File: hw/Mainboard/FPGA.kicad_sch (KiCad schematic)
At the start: 60 parts, among them J16 MCU, J19 PROG, J21 FPGA-P4, J23 FPGA_P2, J24 Conn_02x15_Odd_Even, Q4 MMBT3904, SW5 CONFIG, U21 T8Q144C3

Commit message: hw: add more Mouse part numbers
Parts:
- J16: value MCU -> FPGA_MCU; MOUSER (none) -> 649-1012938195002BLF
- J21: value FPGA-P4 -> FPGA_P3; MOUSER (none) -> 649-1012938195002BLF
- J23: MOUSER (none) -> 649-1012938195002BLF
- J24: value Conn_02x15_Odd_Even -> FPGA_P1; MOUSER (none) -> 649-1012938195002BLF
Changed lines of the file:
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@@
       (effects (font (size 1.27 1.27)) (justify right))
     )
-    (property "Value" "FPGA-P4" (id 1) (at 356.87 152.4 90)
+    (property "Value" "FPGA_P3" (id 1) (at 356.87 152.4 90)
       (effects (font (size 1.27 1.27)) (justify right))
     )
@@
       (effects (font (size 1.27 1.27)) hide)
     )
-    (property "MOUSER" "" (id 5) (at 382.27 162.56 0)
+    (property "MOUSER" "649-1012938195002BLF" (id 5) (at 382.27 162.56 0)
       (effects (font (size 1.27 1.27)) hide)
     )
@@
       (effects (font (size 1.27 1.27)) hide)
     )
-    (property "MOUSER" "" (id 5) (at 384.81 57.15 0)
+    (property "MOUSER" "649-1012938195002BLF" (id 5) (at 384.81 57.15 0)
       (effects (font (size 1.27 1.27)) hide)
     )
@@
     (in_bom yes) (on_board yes) (fields_autoplaced)
     (property "Reference" "J24" (id 0) (at 383.54 82.55 0))
-    (property "Value" "Conn_02x15_Odd_Even" (id 1) (at 383.54 85.09 0))
+    (property "Value" "FPGA_P1" (id 1) (at 383.54 85.09 0))
     (property "Footprint" "Connector_PinHeader_2.54mm:PinHeader_2x15_P2.54mm_Vertical" (id 2) (at 382.27 106.68 0)
       (effects (font (size 1.27 1.27)) hide)
     )
     (property "Datasheet" "" (id 3) (at 382.27 106.68 0)
+      (effects (font (size 1.27 1.27)) hide)
+    )
+    (property "MOUSER" "649-1012938195002BLF" (id 4) (at 382.27 106.68 0)
       (effects (font (size 1.27 1.27)) hide)
     )
@@
     (in_bom yes) (on_board yes) (fields_autoplaced)
     (property "Reference" "J16" (id 0) (at 210.82 35.56 0))
-    (property "Value" "MCU" (id 1) (at 210.82 38.1 0))
+    (property "Value" "FPGA_MCU" (id 1) (at 210.82 38.1 0))
     (property "Footprint" "Connector_PinHeader_2.54mm:PinHeader_2x11_P2.54mm_Vertical" (id 2) (at 209.55 53.34 0)
       (effects (font (size 1.27 1.27)) hide)
@@
       (effects (font (size 1.27 1.27)) hide)
     )
+    (property "MOUSER" "649-1012938195002BLF" (id 4) (at 209.55 53.34 0)
+      (effects (font (size 1.27 1.27)) hide)
+    )

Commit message: hw: PN for IC, remove dup PNs, remove redundant headroom text on PWR
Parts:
- J21, J23: DIGI-KEY SAM1204-14-ND -> (none)
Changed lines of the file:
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@@
-      (effects (font (size 1.27 1.27)) hide)
-    )
-    (property "DIGI-KEY" "SAM1204-14-ND" (id 4) (at 382.27 162.56 0)
       (effects (font (size 1.27 1.27)) hide)
     )
@@
       (effects (font (size 1.27 1.27)) hide)
     )
-    (property "DIGI-KEY" "SAM1204-14-ND" (id 4) (at 384.81 57.15 0)
-      (effects (font (size 1.27 1.27)) hide)
-    )

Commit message: hw: 9V DC plug on left edge, change default track size
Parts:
- renumbered C74 to C31, C60 to C32, C83 to C33, C61 to C34, C66 to C35, C68 to C36, C64 to C37, C63 to C38, C65 to C39, C62 to C40, C67 to C41, C53 to C42, C75 to C43, C71 to C44, C72 to C45, C78 to C46, C34 to C47, C76 to C48, C77 to C49, C79 to C50, C80 to C51, C69 to C52, C73 to C53, D8 to D10, D9 to D11, J19 to J5, J16 to J6, J23 to J7, J24 to J8, J21 to J9, PT41 to PT15, PT42 to PT16, PT43 to PT17, PT44 to PT18, PT45 to PT19, PT46 to PT20, PT48 to PT21, PT47 to PT22, PT40 to PT23, PT54 to PT24, PT53 to PT25, PT52 to PT26, PT51 to PT27, PT50 to PT28, PT49 to PT29, PT39 to PT30, Q4 to Q1, R27 to R20, R33 to R21, R70 to R22, R68 to R23, R71 to R24, R34 to R25, R29 to R26, R30 to R27, R31 to R28, RN14 to RN1, RN15 to RN2, SW5 to SW3, U21 to U10
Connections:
- net GND: no longer PT30.2, U10.1 (GND), U10.104 (GND), U10.108 (GND), U10.120 (GND), U10.121 (GND), U10.126 (GND), U10.127 (GND), U10.129 (GND), U10.133 (GND), U10.37 (GND), U10.44 (GND), U10.5 (GND), U10.50 (GND), U10.64 (GND), U10.9 (GND), U10.94 (GND)
- new net VSS: PT30.2, U10.1 (GND), U10.104 (GND), U10.108 (GND), U10.120 (GND), U10.121 (GND), U10.126 (GND), U10.127 (GND), U10.129 (GND), U10.133 (GND), U10.37 (GND), U10.44 (GND), U10.5 (GND), U10.50 (GND), U10.64 (GND), U10.9 (GND), U10.94 (GND)

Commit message: hw: 25x2 header (wip)
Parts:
- removed J7: FPGA_P2, Connector_PinHeader_2.54mm:PinHeader_2x14_P2.54mm_Vertical, symbol Connector_Generic:Conn_02x14_Odd_Even
- removed J8: FPGA_P1, Connector_PinHeader_2.54mm:PinHeader_2x15_P2.54mm_Vertical, symbol Connector_Generic:Conn_02x15_Odd_Even
- removed J9: FPGA_P3, Connector_PinHeader_2.54mm:PinHeader_2x14_P2.54mm_Vertical, symbol Connector_Generic:Conn_02x14_Odd_Even
- added J5: PMOD1, PET:PMOD_Socket_2x06_P2.54mm_Horizontal, symbol Connector_Generic:Conn_02x06_Top_Bottom
- added J6: PMOD2, PET:PMOD_Socket_2x06_P2.54mm_Horizontal, symbol Connector_Generic:Conn_02x06_Top_Bottom
- added J9: BUS_EXPANSION, Connector_PinHeader_2.54mm:PinHeader_2x25_P2.54mm_Vertical, symbol Connector_Generic:Conn_02x25_Odd_Even
- renumbered J5 to J7, J6 to J8
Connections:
- net +3V3: now also J5.12 (Pin_12), J5.6 (Pin_6), J6.12 (Pin_12), J6.6 (Pin_6), J9.2 (Pin_2)
- net A0: now also U10.58 (GPIOB_RXP02), J9.15 (Pin_15); no longer U10.70 (GPIOB_RXP12_EXTFB0)
- net A1: now also U10.60 (GPIOB_RXN03), J9.17 (Pin_17); no longer U10.72 (GPIOB_CLKN0)
- net A10: now also U10.92 (GPIOR_125_CLK10), J9.35 (Pin_35); no longer U10.105 (GPIOR_95_CDI26)
- net A11: now also U10.98 (GPIOR_117_CTRL14), J9.37 (Pin_37); no longer U10.111 (GPIOR_85)
- net A12: now also U10.59 (GPIOB_RXN02), J9.16 (Pin_16); no longer U10.69 (GPIOB_RXN12_EXTFB0)
- net A13: now also U10.61 (GPIOB_RXP03), J9.18 (Pin_18); no longer U10.71 (GPIOB_CLKP0)
- net A14: now also U10.66 (GPIOB_RXP07), J9.20 (Pin_20); no longer U10.76 (GPIOR_155)
- net A15: now also U10.68 (GPIOB_RXN10), J9.22 (Pin_22); no longer U10.77 (GPIOR_154)
- net A2: now also U10.65 (GPIOB_RXN07), J9.19 (Pin_19); no longer U10.75 (GPIOR_157_PLLIN)
- net A3: now also U10.67 (GPIOB_RXP10), J9.21 (Pin_21); no longer U10.81 (GPIOR_139)
- net A4: now also U10.69 (GPIOB_RXN12_EXTFB0), J9.23 (Pin_23); no longer U10.83 (GPIOR_136_CDI16)
- net A5: now also U10.71 (GPIOB_CLKP0), J9.25 (Pin_25); no longer U10.86 (GPIOR_133_CDI18)
- net A6: now also U10.75 (GPIOR_157_PLLIN), J9.27 (Pin_27); no longer U10.89 (GPIOR_129_CTRL10)
- net A7: now also U10.82 (GPIOR_138), J9.29 (Pin_29); no longer U10.92 (GPIOR_125_CLK10)
- net A8: now also U10.84 (GPIOR_135_CDI17), J9.31 (Pin_31); no longer U10.100 (GPIOR_113_CDI22)
- net A9: now also U10.89 (GPIOR_129_CTRL10), J9.33 (Pin_33); no longer U10.102 (GPIOR_105_CDI24)
- net BE: now also U10.55 (GPIOB_RXP00), J9.12 (Pin_12); no longer U10.67 (GPIOB_RXP10)
- net CBSEL0: no longer U10.137 (GPIOL_70_CBSEL0)
- net CBSEL1: no longer U10.138 (GPIOL_69_CBSEL1)
- net CEC: now also U10.6 (GPIOL_46); no longer U10.4 (GPIOL_54_CDI11)
- net CSI: now also J8.5 (Pin_5)
- net D0: now also U10.76 (GPIOR_155), J9.26 (Pin_26); no longer U10.87 (GPIOR_132_CDI19)
- net D1: now also U10.81 (GPIOR_139), J9.28 (Pin_28); no longer U10.90 (GPIOR_128_CTRL11)
- net D2: now also U10.83 (GPIOR_136_CDI16), J9.30 (Pin_30); no longer U10.93 (GPIOR_123_CLK12_CDI20)
- net D3: now also U10.86 (GPIOR_133_CDI18), J9.32 (Pin_32); no longer U10.101 (GPIOR_112_CDI23)
- net D4: now also U10.90 (GPIOR_128_CTRL11), J9.34 (Pin_34); no longer U10.103 (GPIOR_104_CDI25)
- net D5: now also U10.93 (GPIOR_123_CLK12_CDI20), J9.36 (Pin_36); no longer U10.106 (GPIOR_94_CDI27)
- net D6: now also U10.99 (GPIOR_116_CTRL15), J9.38 (Pin_38); no longer U10.110 (GPIOR_87_CDI29)
- net D7: now also U10.100 (GPIOR_113_CDI22), J9.40 (Pin_40); no longer U10.112 (GPIOR_86)
- net DIAG: now also U10.38 (GPIOB_TXP00); no longer U10.53 (GPIOB_TXP11)
- net GND: now also J9.1 (Pin_1)
- net GRAPHICS: now also U10.40 (GPIOB_TXP02); no longer U10.55 (GPIOB_RXP00)
- net HORIZ: now also U10.109 (GPIOR_88_CDI28); no longer U10.118 (GPIOR_79_EXTFB1_CDI30)
- net I2C0_SCL: now also J8.17 (Pin_17); no longer J8.15 (Pin_15)
- net I2C0_SDA: now also J8.15 (Pin_15); no longer J8.13 (Pin_13)
- net L53: no longer U10.3 (GPIOL_53_CDI10)
- net L64: no longer U10.144 (GPIOL_64)
- net L66: no longer U10.142 (GPIOL_66_CDI12)
- net L75: no longer U10.131 (GPIOL_75_PLLIN1)
- net N00: no longer U10.39 (GPIOB_TXN00)
- net N02: no longer U10.41 (GPIOB_TXN02)
- net N04: no longer U10.43 (GPIOB_TXN04)
- net N06: no longer U10.46 (GPIOB_TXN06)
- net N09: no longer U10.48 (GPIOB_TXN09)
- net P00: no longer U10.38 (GPIOB_TXP00)
- net P02: no longer U10.40 (GPIOB_TXP02)
- net P04: no longer U10.42 (GPIOB_TXP04)
- net P06: no longer U10.45 (GPIOB_TXP06)
- net P09: no longer U10.47 (GPIOB_TXP09)
- net PHI2: now also U10.54 (GPIOB_TXN11), J9.11 (Pin_11); no longer U10.97 (GPIOR_122_CLK13_CDI21)
- net R76: no longer U10.124 (GPIOR_76_PLLIN0)
- net RAM_A10: now also U10.101 (GPIOR_112_CDI23); no longer U10.109 (GPIOR_88_CDI28)
- net RAM_A11: now also U10.97 (GPIOR_122_CLK13_CDI21); no longer U10.113 (GPIOR_84)
- net RAM_A15: now also U10.77 (GPIOR_154); no longer U10.82 (GPIOR_138)
- net RAM_A16: now also U10.70 (GPIOB_RXP12_EXTFB0), J9.24 (Pin_24); no longer U10.84 (GPIOR_135_CDI17)
- net RDY: now also U10.42 (GPIOB_TXP04), J9.4 (Pin_4); no longer U10.60 (GPIOB_RXN03)
- net R~{W}: now also U10.56 (GPIOB_RXN00), J9.13 (Pin_13); no longer U10.99 (GPIOR_116_CTRL15)
- net S1: now also U10.123 (GPIOR_77_PLLIN1); no longer U10.134 (GPIOL_73_EXTFB1_CDI15)
- net S2: now also U10.124 (GPIOR_76_PLLIN0); no longer U10.135 (GPIOL_72_EXTFB0_CDI14)
- net S3: now also U10.131 (GPIOL_75_PLLIN1); no longer U10.139 (GPIOL_68)
- net S4: now also U10.134 (GPIOL_73_EXTFB1_CDI15); no longer U10.140 (GPIOL_67_CDI13)
- net SPI0_RX: now also J8.13 (Pin_13); no longer J8.11 (Pin_11)
- net SPI0_SCK: now also J8.9 (Pin_9); no longer J8.7 (Pin_7)
- net SPI0_TX: now also J8.11 (Pin_11); no longer J8.9 (Pin_9)
- net SPI0_~{CS}: now also J8.7 (Pin_7); no longer J8.5 (Pin_5)
- net SYNC: now also U10.47 (GPIOB_TXP09), J9.8 (Pin_8); no longer U10.68 (GPIOB_RXN10)
- net VERT: now also U10.105 (GPIOR_95_CDI26), J9.47 (Pin_47); no longer U10.116 (GPIOR_81_MREFCLK)
- net VIA_CB2: now also U10.39 (GPIOB_TXN00); no longer U10.54 (GPIOB_TXN11)
- net VIDEO: now also U10.102 (GPIOR_105_CDI24); no longer U10.114 (GPIOR_83)
- net ~{IO_OE}: now also U10.110 (GPIOR_87_CDI29); no longer U10.119 (GPIOR_78_EXTFB0_CDI31)
- net ~{IRQ}: now also U10.43 (GPIOB_TXN04), J9.5 (Pin_5); no longer U10.65 (GPIOB_RXN07)
- net ~{ML}: now also U10.45 (GPIOB_TXP06), J9.6 (Pin_6); no longer U10.66 (GPIOB_RXP07)
- net ~{NMI}: now also U10.46 (GPIOB_TXN06), J9.7 (Pin_7); no longer U10.141 (GPIOL_65)
- net ~{PIA1_CS}: now also U10.103 (GPIOR_104_CDI25); no longer U10.115 (GPIOR_82)
- net ~{PIA2_CS}: now also U10.111 (GPIOR_85); no longer U10.123 (GPIOR_77_PLLIN1)
- net ~{RAM_OE}: now also U10.87 (GPIOR_132_CDI19); no longer U10.56 (GPIOB_RXN00)
- net ~{RAM_WE}: now also U10.72 (GPIOB_CLKN0); no longer U10.58 (GPIOB_RXP02)
- net ~{RES}: now also U10.48 (GPIOB_TXN09), J9.9 (Pin_9); no longer U10.98 (GPIOR_117_CTRL14)
- net ~{SO}: now also U10.53 (GPIOB_TXP11), J9.10 (Pin_10); no longer U10.61 (GPIOB_RXP03)
- net ~{VIA_CS}: now also U10.106 (GPIOR_94_CDI27); no longer U10.117 (GPIOR_80)
- net ~{VP}: now also U10.41 (GPIOB_TXN02), J9.3 (Pin_3); no longer U10.59 (GPIOB_RXN02)
- removed net L46: J8.17 (Pin_17), U10.6 (GPIOL_46)
- new net PD_GND: J5.11 (Pin_11), J5.5 (Pin_5), J6.11 (Pin_11), J6.5 (Pin_5)
- new net PMOD1_1: J5.1 (Pin_1), U10.112 (GPIOR_86)
- new net PMOD1_2: J5.2 (Pin_2), U10.114 (GPIOR_83)
- new net PMOD1_3: J5.3 (Pin_3), U10.116 (GPIOR_81_MREFCLK)
- new net PMOD1_4: J5.4 (Pin_4), U10.118 (GPIOR_79_EXTFB1_CDI30)
- new net PMOD1_5: J5.7 (Pin_7), U10.113 (GPIOR_84)
- new net PMOD1_6: J5.8 (Pin_8), U10.115 (GPIOR_82)
- new net PMOD1_7: J5.9 (Pin_9), U10.117 (GPIOR_80)
- new net PMOD1_8: J5.10 (Pin_10), U10.119 (GPIOR_78_EXTFB0_CDI31)
- new net PMOD2_1: J6.1 (Pin_1), U10.137 (GPIOL_70_CBSEL0)
- new net PMOD2_2: J6.2 (Pin_2), U10.139 (GPIOL_68)
- new net PMOD2_3: J6.3 (Pin_3), U10.142 (GPIOL_66_CDI12)
- new net PMOD2_4: J6.4 (Pin_4), U10.144 (GPIOL_64)
- new net PMOD2_5: J6.7 (Pin_7), U10.135 (GPIOL_72_EXTFB0_CDI14)
- new net PMOD2_6: J6.8 (Pin_8), U10.138 (GPIOL_69_CBSEL1)
- new net PMOD2_7: J6.9 (Pin_9), U10.140 (GPIOL_67_CDI13)
- new net PMOD2_8: J6.10 (Pin_10), U10.141 (GPIOL_65)
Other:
- moved on the sheet: U10I

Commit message: hw: 2x config switch (wip)
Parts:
- SW3: footprint Button_Switch_THT:SW_DIP_SPSTx04_Slide_6.7x11.72mm_W7.62mm_P2.54mm_LowProfile -> Button_Switch_THT:SW_DIP_SPSTx02_Slide_6.7x6.64mm_W7.62mm_P2.54mm_LowProfile; symbol Switch:SW_DIP_x04 -> Switch:SW_DIP_x02; MOUSER 490-DS04-254-1L-04BK -> (none)
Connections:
- net GND: no longer SW3.3, SW3.4
- net S1: now also SW3.4; no longer SW3.8
- net S2: now also SW3.3; no longer SW3.7
- net S3: no longer SW3.6
- net S4: no longer SW3.5

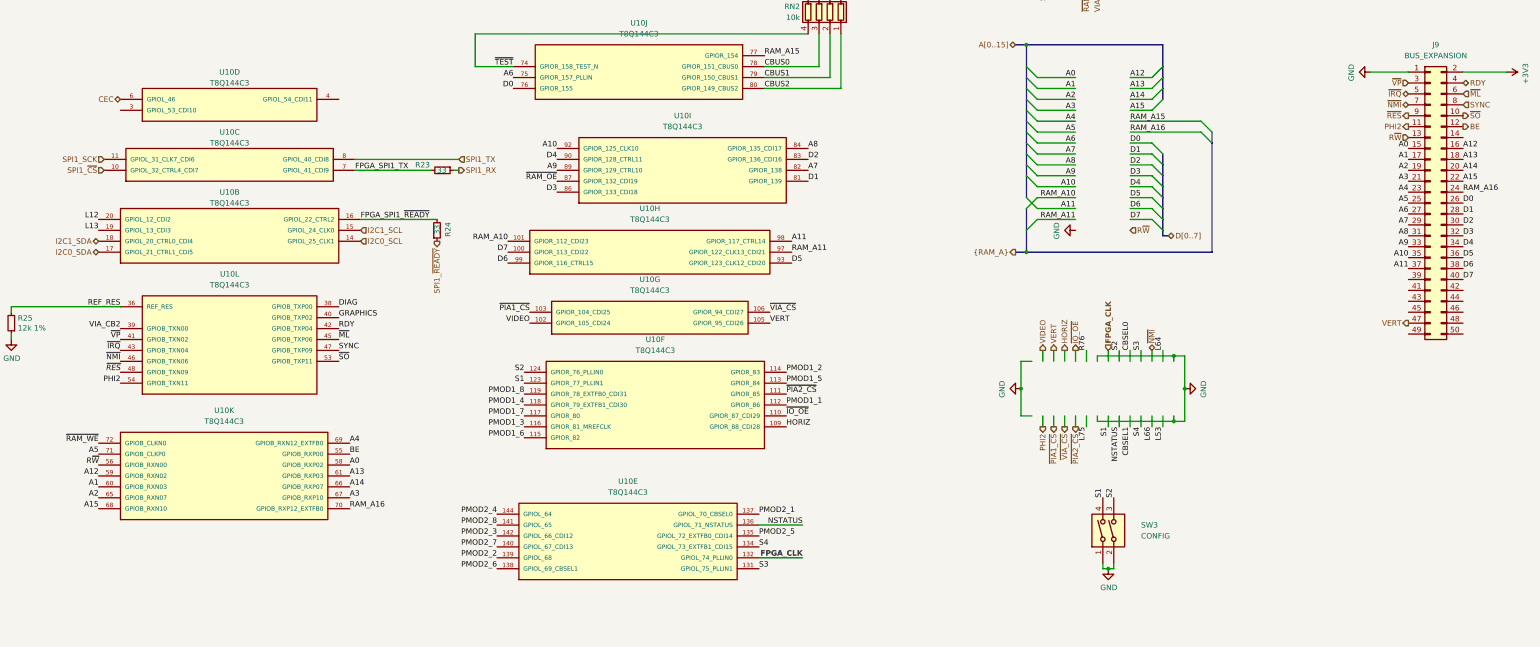
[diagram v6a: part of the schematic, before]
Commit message: hw: reorder CPU breakout pins
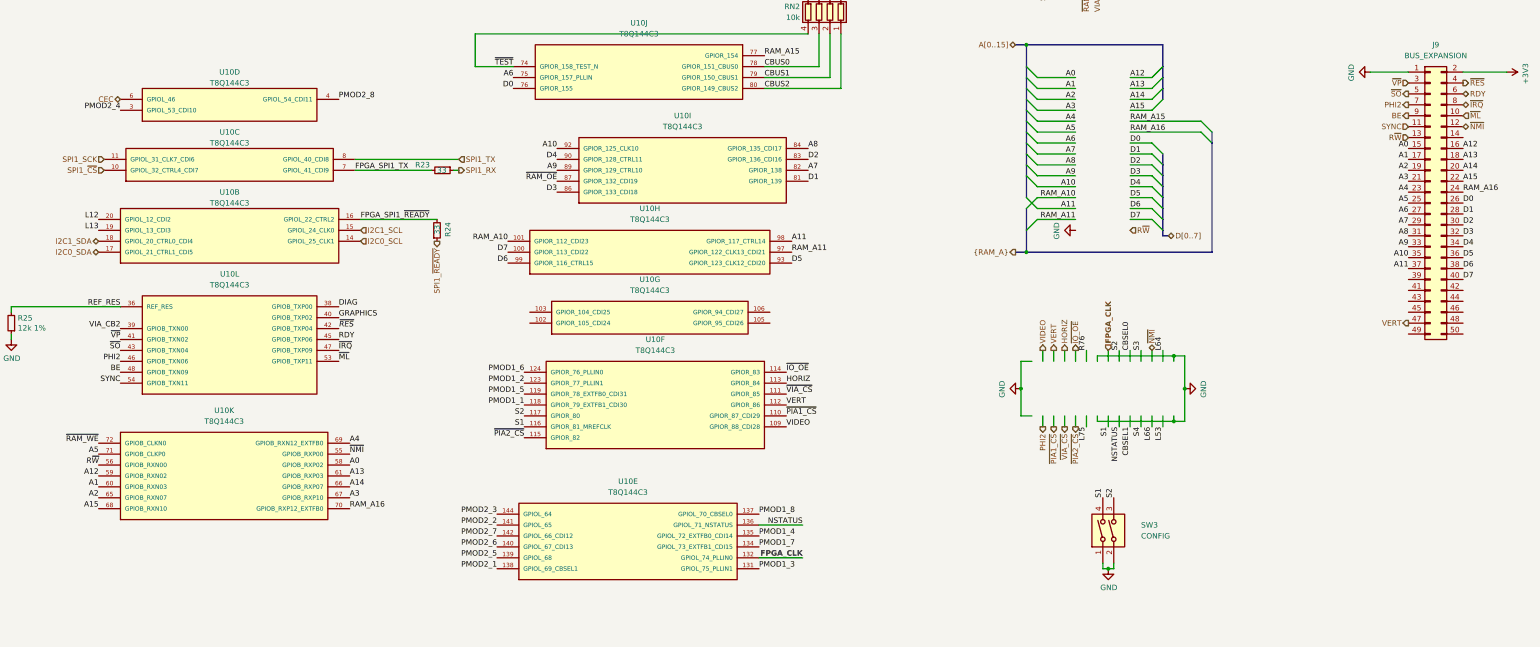
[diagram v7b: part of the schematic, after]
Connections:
- net BE: now also J9.9 (Pin_9), U10.48 (GPIOB_TXN09); no longer J9.12 (Pin_12), U10.55 (GPIOB_RXP00)
- net HORIZ: now also U10.113 (GPIOR_84); no longer U10.109 (GPIOR_88_CDI28)
- net PHI2: now also J9.7 (Pin_7), U10.46 (GPIOB_TXN06); no longer J9.11 (Pin_11), U10.54 (GPIOB_TXN11)
- net PMOD1_1: now also U10.118 (GPIOR_79_EXTFB1_CDI30); no longer U10.112 (GPIOR_86)
- net PMOD1_2: now also U10.123 (GPIOR_77_PLLIN1); no longer U10.114 (GPIOR_83)
- net PMOD1_3: now also U10.131 (GPIOL_75_PLLIN1); no longer U10.116 (GPIOR_81_MREFCLK)
- net PMOD1_4: now also U10.135 (GPIOL_72_EXTFB0_CDI14); no longer U10.118 (GPIOR_79_EXTFB1_CDI30)
- net PMOD1_5: now also U10.119 (GPIOR_78_EXTFB0_CDI31); no longer U10.113 (GPIOR_84)
- net PMOD1_6: now also U10.124 (GPIOR_76_PLLIN0); no longer U10.115 (GPIOR_82)
- net PMOD1_7: now also U10.134 (GPIOL_73_EXTFB1_CDI15); no longer U10.117 (GPIOR_80)
- net PMOD1_8: now also U10.137 (GPIOL_70_CBSEL0); no longer U10.119 (GPIOR_78_EXTFB0_CDI31)
- net PMOD2_1: now also U10.138 (GPIOL_69_CBSEL1); no longer U10.137 (GPIOL_70_CBSEL0)
- net PMOD2_2: now also U10.141 (GPIOL_65); no longer U10.139 (GPIOL_68)
- net PMOD2_3: now also U10.144 (GPIOL_64); no longer U10.142 (GPIOL_66_CDI12)
- net PMOD2_4: now also U10.3 (GPIOL_53_CDI10); no longer U10.144 (GPIOL_64)
- net PMOD2_5: now also U10.139 (GPIOL_68); no longer U10.135 (GPIOL_72_EXTFB0_CDI14)
- net PMOD2_6: now also U10.140 (GPIOL_67_CDI13); no longer U10.138 (GPIOL_69_CBSEL1)
- net PMOD2_7: now also U10.142 (GPIOL_66_CDI12); no longer U10.140 (GPIOL_67_CDI13)
- net PMOD2_8: now also U10.4 (GPIOL_54_CDI11); no longer U10.141 (GPIOL_65)
- net RDY: now also J9.6 (Pin_6), U10.45 (GPIOB_TXP06); no longer J9.4 (Pin_4), U10.42 (GPIOB_TXP04)
- net S1: now also U10.116 (GPIOR_81_MREFCLK); no longer U10.123 (GPIOR_77_PLLIN1)
- net S2: now also U10.117 (GPIOR_80); no longer U10.124 (GPIOR_76_PLLIN0)
- net S3: no longer U10.131 (GPIOL_75_PLLIN1)
- net S4: no longer U10.134 (GPIOL_73_EXTFB1_CDI15)
- net SYNC: now also J9.11 (Pin_11), U10.54 (GPIOB_TXN11); no longer J9.8 (Pin_8), U10.47 (GPIOB_TXP09)
- net VERT: now also U10.112 (GPIOR_86); no longer U10.105 (GPIOR_95_CDI26)
- net VIDEO: now also U10.109 (GPIOR_88_CDI28); no longer U10.102 (GPIOR_105_CDI24)
- net ~{IO_OE}: now also U10.114 (GPIOR_83); no longer U10.110 (GPIOR_87_CDI29)
- net ~{IRQ}: now also J9.8 (Pin_8), U10.47 (GPIOB_TXP09); no longer J9.5 (Pin_5), U10.43 (GPIOB_TXN04)
- net ~{ML}: now also J9.10 (Pin_10), U10.53 (GPIOB_TXP11); no longer J9.6 (Pin_6), U10.45 (GPIOB_TXP06)
- net ~{NMI}: now also J9.12 (Pin_12), U10.55 (GPIOB_RXP00); no longer J9.7 (Pin_7), U10.46 (GPIOB_TXN06)
- net ~{PIA1_CS}: now also U10.110 (GPIOR_87_CDI29); no longer U10.103 (GPIOR_104_CDI25)
- net ~{PIA2_CS}: now also U10.115 (GPIOR_82); no longer U10.111 (GPIOR_85)
- net ~{RES}: now also J9.4 (Pin_4), U10.42 (GPIOB_TXP04); no longer J9.9 (Pin_9), U10.48 (GPIOB_TXN09)
- net ~{SO}: now also J9.5 (Pin_5), U10.43 (GPIOB_TXN04); no longer J9.10 (Pin_10), U10.53 (GPIOB_TXP11)
- net ~{VIA_CS}: now also U10.111 (GPIOR_85); no longer U10.106 (GPIOR_94_CDI27)
